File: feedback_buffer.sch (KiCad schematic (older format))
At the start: 23 parts, among them IC1 DAC53401DSGR, U14 DG412xUE, U15 OPA828, U23 OPA188xxDBV

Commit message: updating git so that kicad schematic matches pdf doc
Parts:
- IC1: Manf# (none) -> DAC53401DSGR
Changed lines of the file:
@@
 F 10 "DAC53401DSGR" H 5050 4300 50  0001 L CNN "Arrow Part Number"
 F 11 "https://www.arrow.com/en/products/dac53401dsgr/texas-instruments" H 5050 4200 50  0001 L CNN "Arrow Price/Stock"
+F 12 "DAC53401DSGR" H 4000 5000 50  0001 C CNN "Manf#"
 	1    4000 5000
 	1    0    0    -1

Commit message: added many alternate manufacturing part numbers
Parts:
- removed C19: 2.2u, Capacitor_SMD:C_0603_1608Metric, symbol Device:C
- removed IC1: DAC53401DSGR, covg-kicad:WSON-8-1EP_2x2mm_P0.5mm_EP0.9x1.6mm_posMask, symbol covg-kicad:DAC53401DSGR
- added U?: DAC101C081CIMK_NOPB, Package_TO_SOT_SMD:TSOT-23-6_HandSoldering, symbol covg-kicad:DAC101C081CIMK_NOPB
- U14: Alternate Manf# (none) -> TMUX6111PWR; Alternate2 Manf# (none) -> TMUX6112PWR; Alternate3 Manf# (none) -> TMUX6113PWR
- U15: Alternate Manf# (none) -> OPA1641AIDR; Alternate2 Manf# (none) -> OPA1655DR; Alternate3 Manf# (none) -> ADA4625-1ARDZ-R7; Alternate4 Manf# (none) -> AD820BRZ
- U23: Alternate Manf# (none) -> OPA180IDBVT; Alternate2 Manf# (none) -> OPA202IDBVT
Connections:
- net labels added: 3V3_BUF
- net labels removed: +3.3V
- wire segments 99 -> 91
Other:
- note added: "A0 to VDD, Float, Gnd\n\n0x0D = 7b0001101 when A0 = Gnd\n(and avoid) 0x44 = 7b1000100\n\nTable 1 in datasheet is confusing: \nsee Ti Forum “DAC101C081: DAC101C081 I2C address selection”\nAvoid the 2nd address in the Slave Address column"
- note removed: "A0 to AGND, VDD, SCL or SDA\n\n0x48 = ‘b1001000 (7-bit) with AGND"
- note removed: "Use internal reference (1.20 V)\nGain = x1"
- moved on the sheet: C20, R31, R47

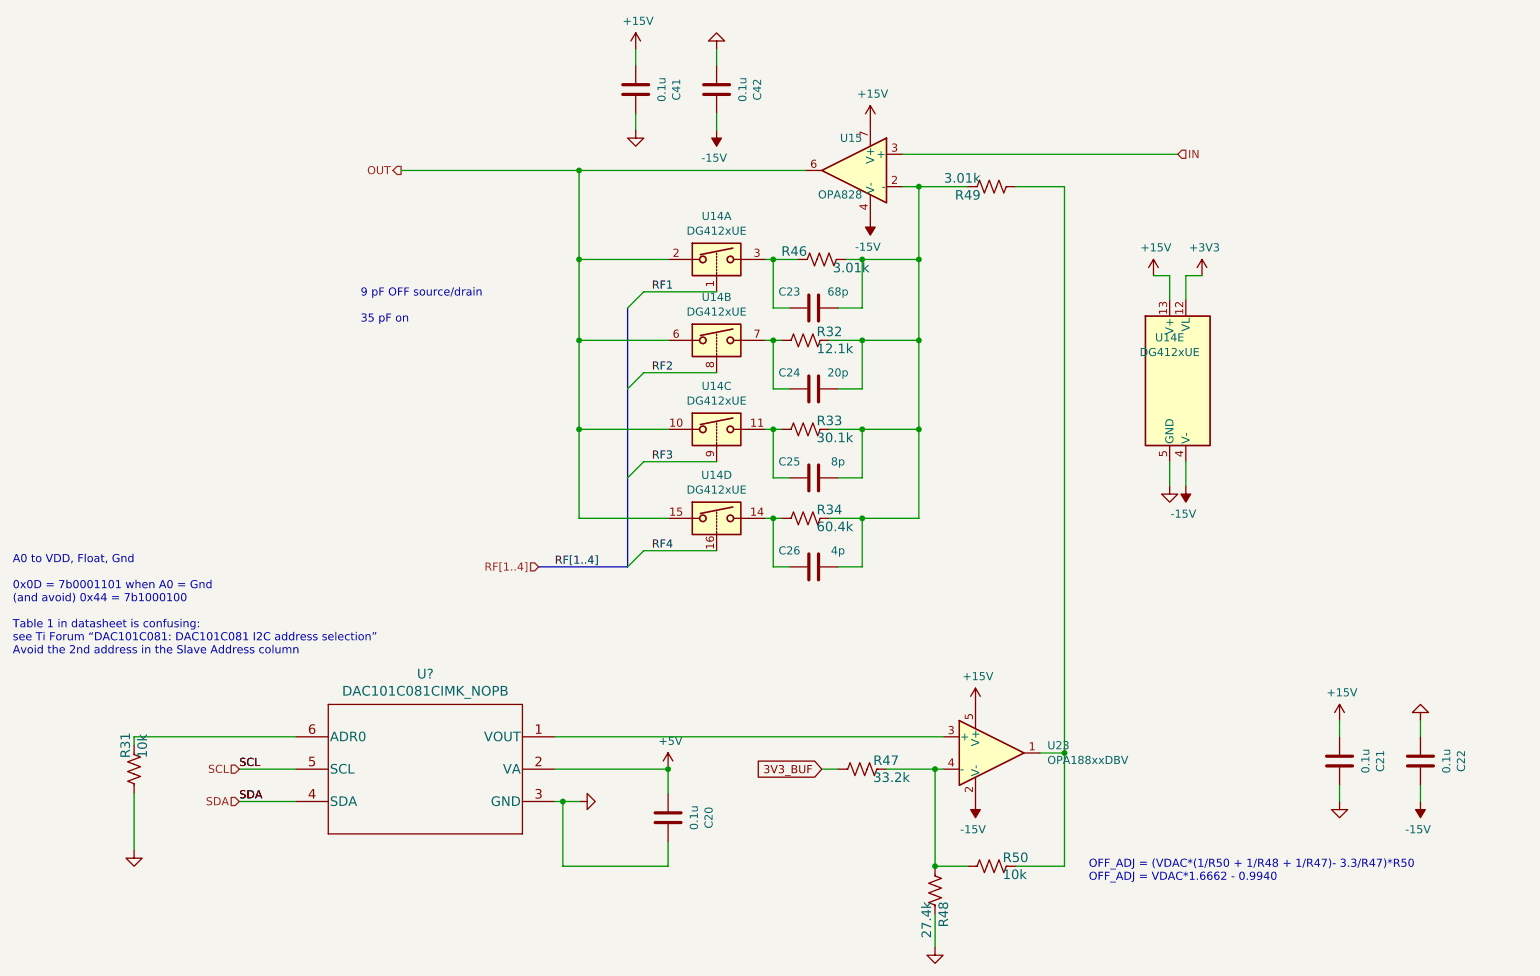
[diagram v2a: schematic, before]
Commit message: updates to schematic for alternate part #s
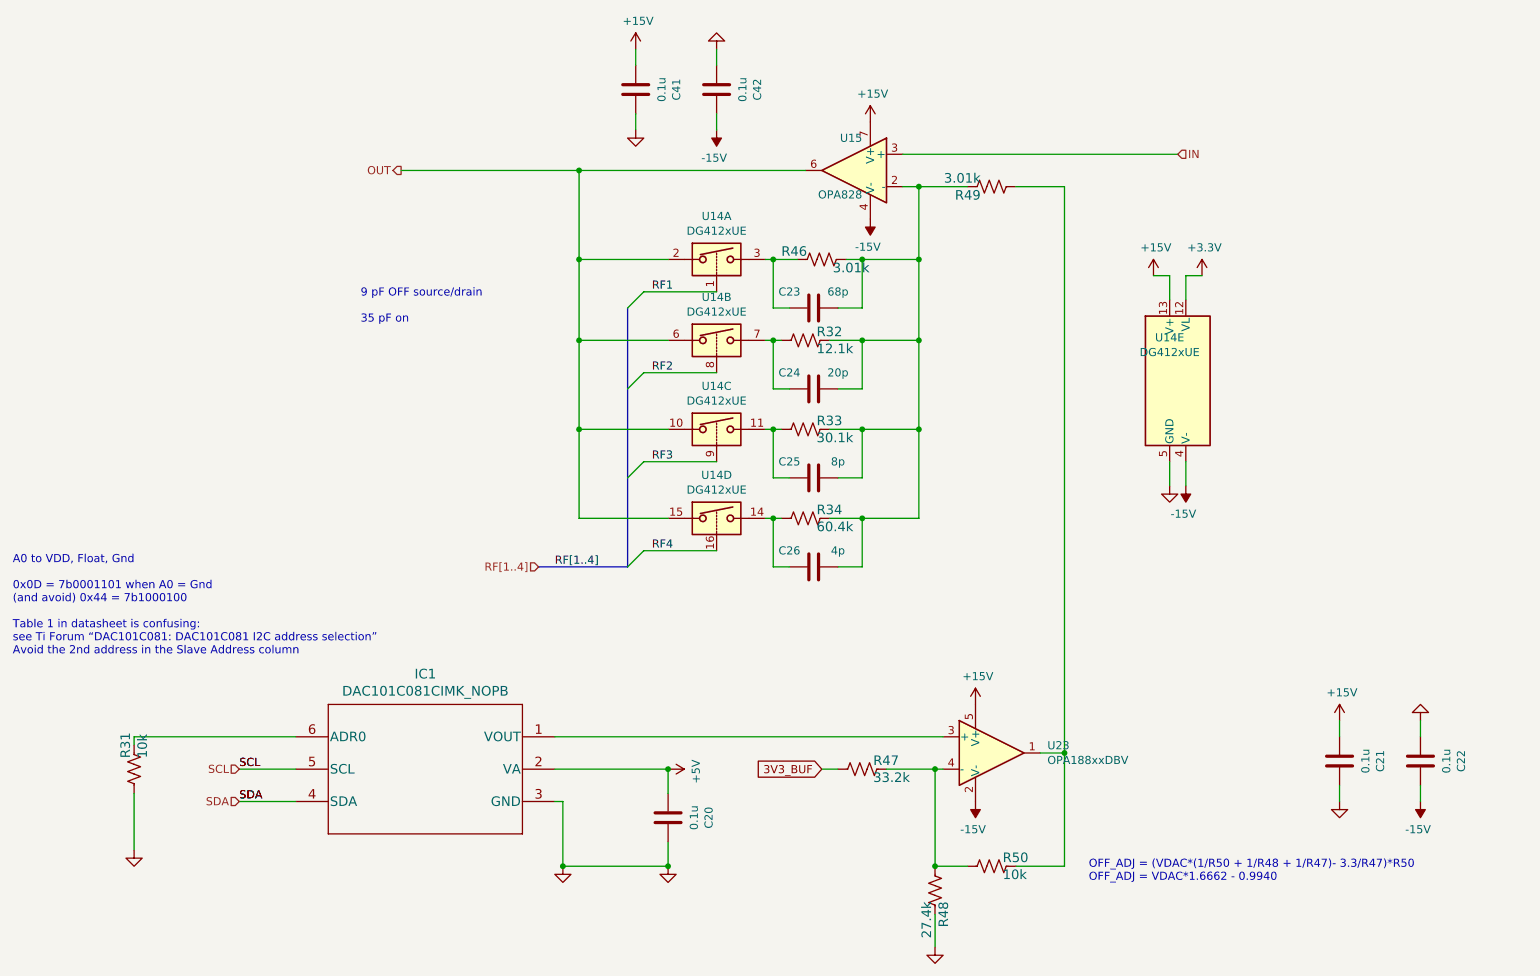
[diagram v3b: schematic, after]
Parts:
- gave numbers to parts that had none: 1
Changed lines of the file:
@@
 L power:GND #PWR?
 U 1 1 62160D82
-P 4100 5400
+P 4000 5800
 AR Path="/6032F251/62160D82" Ref="#PWR?"  Part="1"
 AR Path="/6032F251/62017813/62160D82" Ref="#PWR0109"  Part="1"
-F 0 "#PWR0109" H 4100 5150 50  0001 C CNN
-F 1 "GND" V 4105 5272 50  0001 R CNN
-F 2 "" H 4100 5400 50  0001 C CNN
-F 3 "" H 4100 5400 50  0001 C CNN
-	1    4100 5400
-	0    -1   -1   0
+F 0 "#PWR0109" H 4000 5550 50  0001 C CNN
+F 1 "GND" V 4005 5672 50  0001 R CNN
+F 2 "" H 4000 5800 50  0001 C CNN
+F 3 "" H 4000 5800 50  0001 C CNN
+	1    4000 5800
+	1    0    0    -1
 $EndComp
 $Comp
@@
 F 3 "" H 4650 5200 50  0001 C CNN
 	1    4650 5200
-	1    0    0    -1
+	0    1    1    0
 $EndComp
 $Comp
@@
 	1    0    0    -1
 $EndComp
-$Comp
-L power:+3V3 #PWR0188
-U 1 1 60EA1A48
-P 7950 2150
-F 0 "#PWR0188" H 7950 2000 50  0001 C CNN
-F 1 "+3V3" H 7965 2323 50  0000 C CNN
-F 2 "" H 7950 2150 50  0001 C CNN
-F 3 "" H 7950 2150 50  0001 C CNN
-	1    7950 2150
-	1    0    0    -1
-$EndComp
 Wire Wire Line
 	7850 2150 7850 2300
@@
 Connection ~ 4650 5200
 $Comp
-L covg-kicad:DAC101C081CIMK_NOPB U?
+L covg-kicad:DAC101C081CIMK_NOPB IC1
 U 1 1 625C94E3
 P 3150 5200
-F 0 "U?" H 3150 5788 60  0000 C CNN
+F 0 "IC1" H 3150 5788 60  0000 C CNN
 F 1 "DAC101C081CIMK_NOPB" H 3150 5682 60  0000 C CNN
 F 2 "Package_TO_SOT_SMD:TSOT-23-6_HandSoldering" H 3150 5140 60  0001 C CNN
@@
 	3950 5200 4650 5200
 Wire Wire Line
-	4100 5400 4000 5400
-Wire Wire Line
 	3950 5000 6350 5000
 Wire Wire Line
@@
 Wire Wire Line
 	4000 5800 4650 5800
-Connection ~ 4000 5400
 Wire Wire Line
 	4000 5400 3950 5400
@@
 P 1350 5700
 AR Path="/6032F251/62621C47" Ref="#PWR?"  Part="1"
-AR Path="/6032F251/62017813/62621C47" Ref="#PWR?"  Part="1"
-F 0 "#PWR?" H 1350 5450 50  0001 C CNN
+AR Path="/6032F251/62017813/62621C47" Ref="#PWR0210"  Part="1"
+F 0 "#PWR0210" H 1350 5450 50  0001 C CNN
 F 1 "GND" V 1355 5572 50  0001 R CNN
 F 2 "" H 1350 5700 50  0001 C CNN
@@
 Wire Wire Line
 	6300 6100 6300 6300
+$Comp
+L power:+3.3V #PWR?
+U 1 1 626368C5
+P 7950 2150
+F 0 "#PWR?" H 7950 2000 50  0001 C CNN
+F 1 "+3.3V" H 7965 2323 50  0000 C CNN
+F 2 "" H 7950 2150 50  0001 C CNN
+F 3 "" H 7950 2150 50  0001 C CNN
+	1    7950 2150
+	1    0    0    -1
+$EndComp
+Connection ~ 4000 5800
+$Comp
+L power:GND #PWR?
+U 1 1 6263B929
+P 4650 5800
+AR Path="/6032F251/6263B929" Ref="#PWR?"  Part="1"
+AR Path="/6032F251/62017813/6263B929" Ref="#PWR?"  Part="1"
+F 0 "#PWR?" H 4650 5550 50  0001 C CNN
+F 1 "GND" V 4655 5672 50  0001 R CNN
+F 2 "" H 4650 5800 50  0001 C CNN
+F 3 "" H 4650 5800 50  0001 C CNN
+	1    4650 5800
+	1    0    0    -1
+$EndComp
+Connection ~ 4650 5800
 Wire Bus Line
 	4400 2350 4400 3950

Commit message: gerbers, BOM and fabrication files sent to PCBway
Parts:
- U14: Alternate Manf# (none) -> TMUX6111PWR; Alternate2 Manf# (none) -> TMUX6112PWR
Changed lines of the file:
@@
 F 3 "https://datasheets.maximintegrated.com/en/ds/DG411-DG413.pdf" H 7750 2800 50  0001 C CNN
 F 4 "DG412CUE+" H 7750 2800 50  0001 C CNN "Manf#"
+F 5 "TMUX6111PWR" H 7750 2800 50  0001 C CNN "Alternate Manf#"
+F 6 "TMUX6112PWR" H 7750 2800 50  0001 C CNN "Alternate2 Manf#"
 	5    7750 2800
 	1    0    0    -1
